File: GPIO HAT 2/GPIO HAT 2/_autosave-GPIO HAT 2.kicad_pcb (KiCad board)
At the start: 4 copper layers, 85 x 74.7 mm, 109 parts, among them J1 ., J10 ., J11 ., J12 ., J13 ., J14 ., J15 ., J16 ., J17 ., J18 ., J19 ., J2 ., J20 ., J21 LVDS, J22 LVDS, J23 02x02, J24 USB_C_Receptacle_PowerOnly_6P, J25 SMD PAD, J3 ., J4 ., J5 ., J6 ., J7 ., J8 ., J9 ., U1 TXB0108DQSR, U10 TXB0108DQSR, U12 SY8088IAAC, U13 SY8088IAAC, U14 TPS2117, U2 TXB0108DQSR, U3 TXB0108DQSR, U4 TXB0108DQSR, U5 TXB0108DQSR, U6 TXB0108DQSR, U7 TXB0108DQSR, U8 TXB0108DQSR, U9 TXB0108DQSR

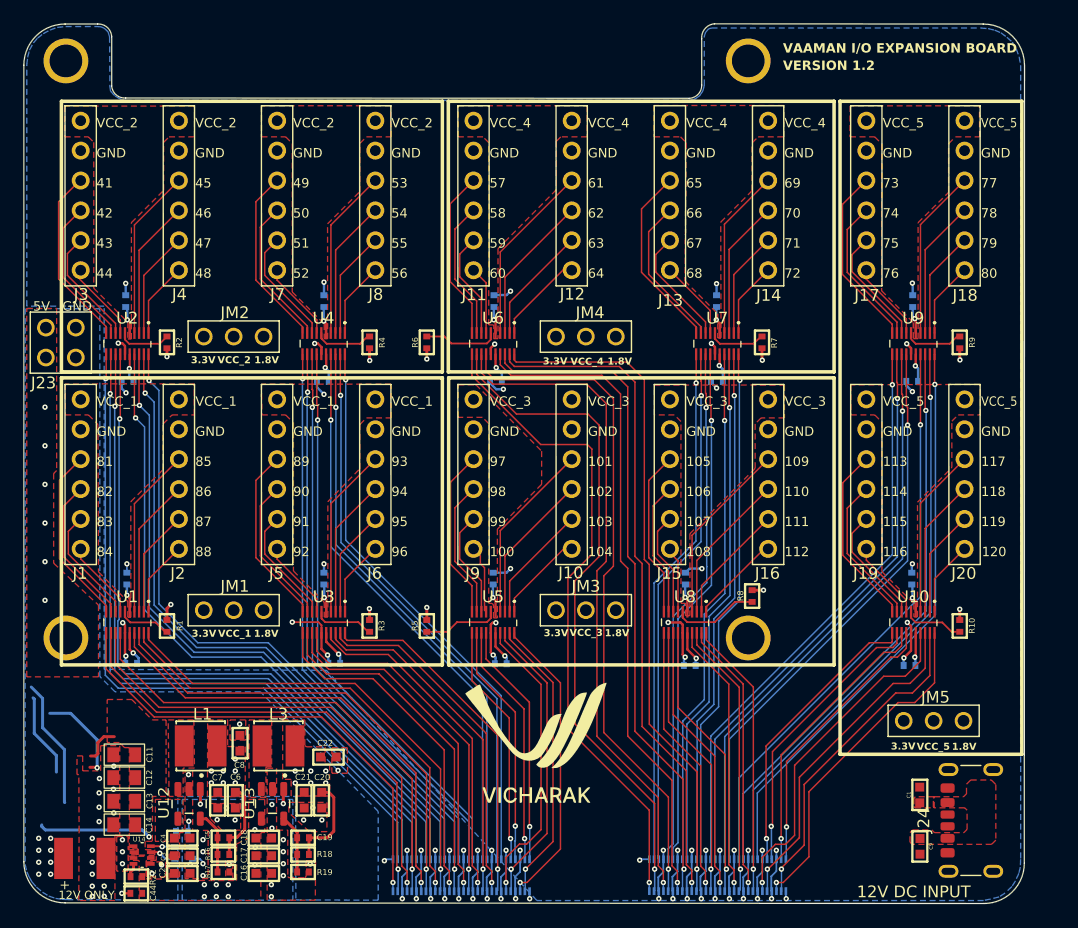
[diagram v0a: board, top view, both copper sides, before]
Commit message: 12V Jack removed and 5V USB added
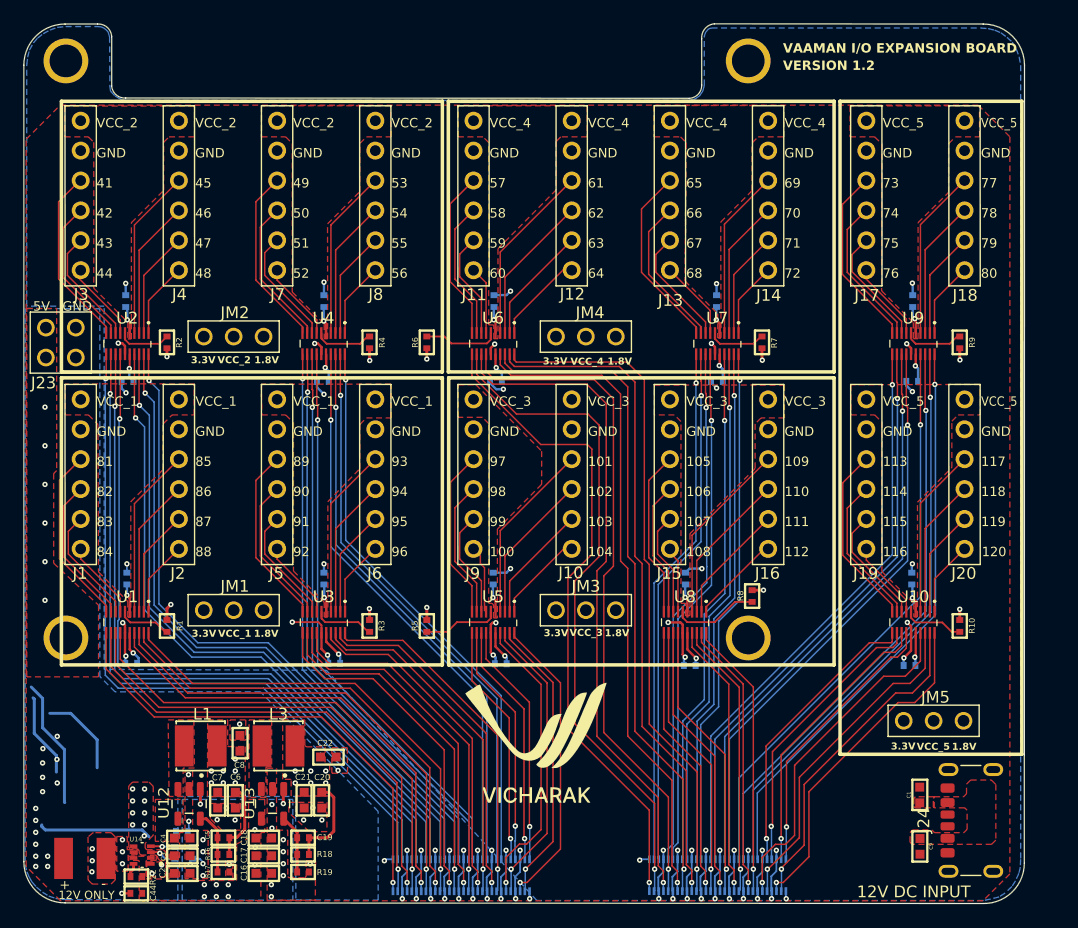
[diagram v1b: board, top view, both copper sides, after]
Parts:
- removed C11, C12, C13, C14: 22uF, VAAMAN2:0805_Cap
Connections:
- J25 pad 1: 5V_1 -> GND
- J25 pad 2: GND -> 5V_1
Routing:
- net (no net): track 26.1 -> 18.3 mm, vias 1 -> 0
- net GND: track 129.0 -> 136.1 mm
- net 5V_1: track 15.1 -> 11.9 mm, vias 10 -> 13
- added copper zone on In2.Cu, net 5V_1
- removed copper zone on In2.Cu, net 5V
